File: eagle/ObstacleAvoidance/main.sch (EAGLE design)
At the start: 16 parts, among them IC1 L293D, X1 JST-XH-02-PIN-LONG-PAD, X2 JST-XH-02-PIN-LONG-PAD

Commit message: Feat: Eagle pcb
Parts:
- added J1, J2: (no value), jumper:J2X5MM
- added LED2: TLLG4400, led:TLLG4400
- added R3: 1k, rcl:R-EU_0207/10
- added U$8: ULTRASONIC-HC-SR04#V, diy-modules:ULTRASONIC-HC-SR04#V
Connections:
- new net 12V-VCC2: IC1.VCC2, J2.3, R3.1
- new net ECHO-F: U$1.IO26, U$8.ECHO
- new net N$7: C1.1, J1.2, U$7.IN
- new net N$9: LED2.A, R3.2
- new net TRIG-F: U$1.IO27, U$8.TRIG
- net 12V: now also J2.2; no longer IC1.VCC2
- net 3.3V: now also U$8.VCC
- net 8V: now also J1.3; no longer C1.1, U$7.IN
- net ECHO-L: now also U$1.IO17; no longer U$1.IO16
- net GND: now also LED2.C, U$8.GND
- net IN1-A: now also U$1.IO33; no longer U$1.IO26
- net IN2-A: now also U$1.IO32; no longer U$1.IO27
- net TRIG-L: now also U$1.IO16; no longer U$1.IO17
- net VOLT: now also U$1.IO22; no longer U$1.IO13
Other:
- moved on the sheet: U$3

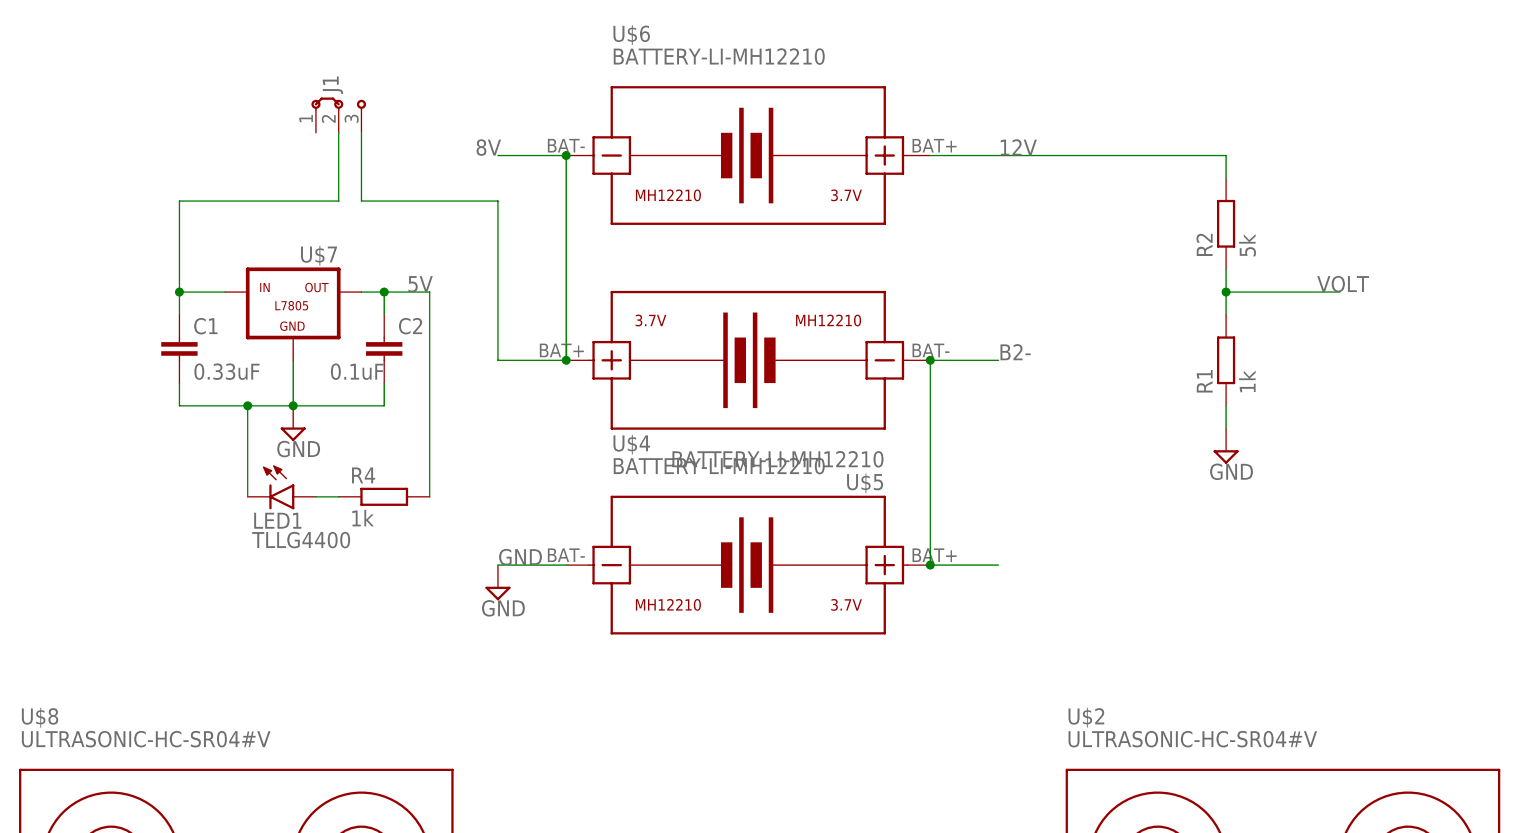
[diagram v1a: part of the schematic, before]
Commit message: Feat: PCB battery connector
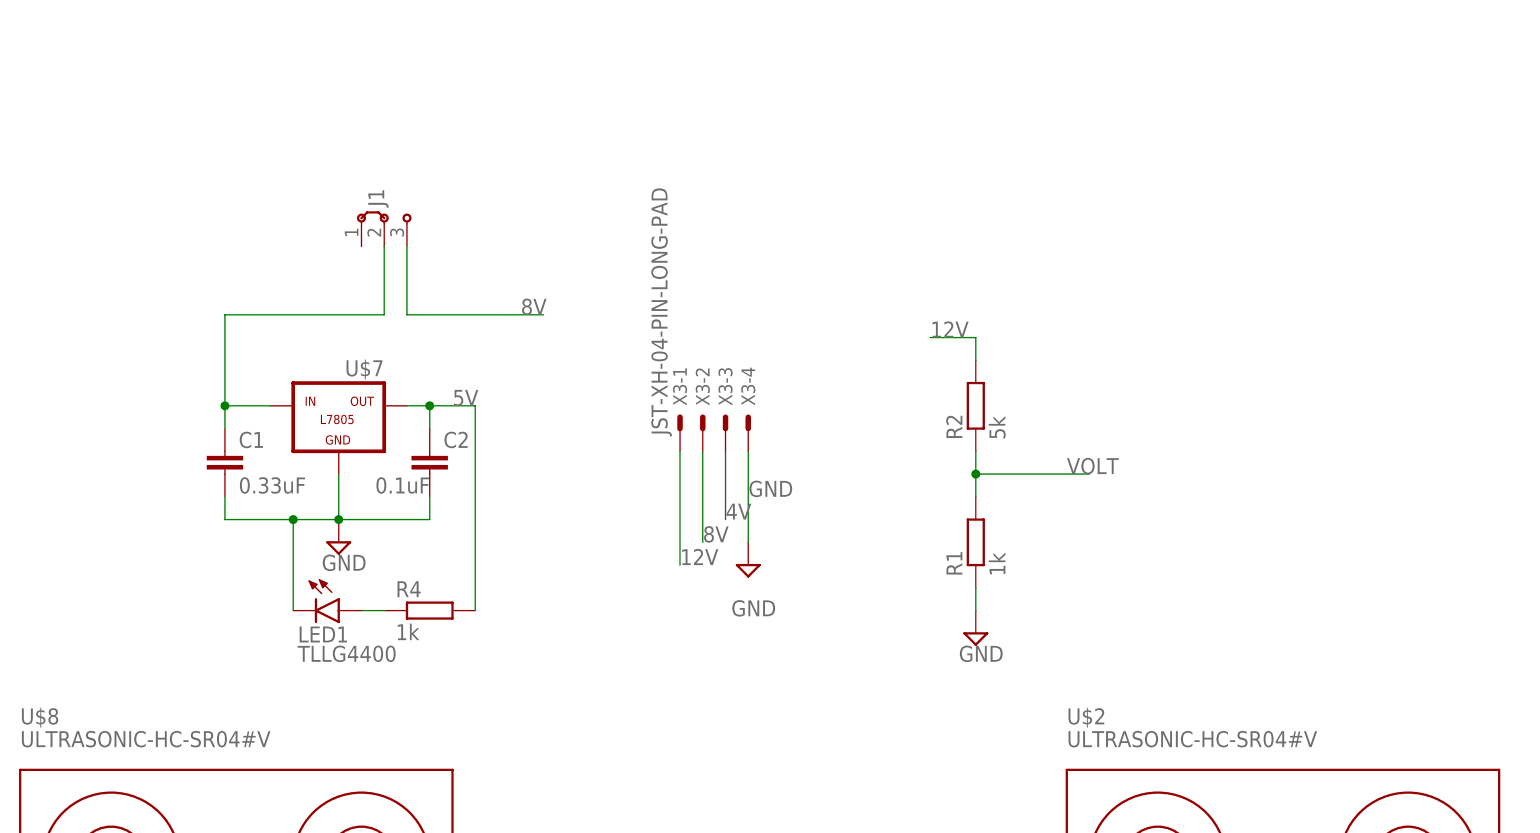
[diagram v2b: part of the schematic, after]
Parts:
- removed U$4, U$5, U$6: BATTERY-LI-MH12210, diy-modules:BATTERY-LI-MH12210
- added X3: JST-XH-04-PIN-LONG-PAD, Rembrandt Electronics - JST XH Connectors v1-0:JST-XH-04-PIN-LONG-PAD
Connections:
- removed net B2-: U$4.BAT+, U$5.BAT-
- new net 4V: X3-3.S
- net 12V: now also X3-1.S; no longer U$6.BAT+
- net 8V: now also X3-2.S; no longer U$5.BAT+, U$6.BAT-
- net GND: now also X3-4.S; no longer U$4.BAT-
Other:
- moved on the sheet: C1, C2, J1, LED1, R1, R2, R4, U$7
